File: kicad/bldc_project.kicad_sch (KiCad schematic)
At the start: 33 parts, among them Q1 IRFZ44N, Q2 IRFZ44N, Q3 IRFZ44N, Q4 IRFZ44N, Q5 IRFZ44N, Q6 IRFZ44N, U1 IR2104, U2 IR2104, U3 IR2104

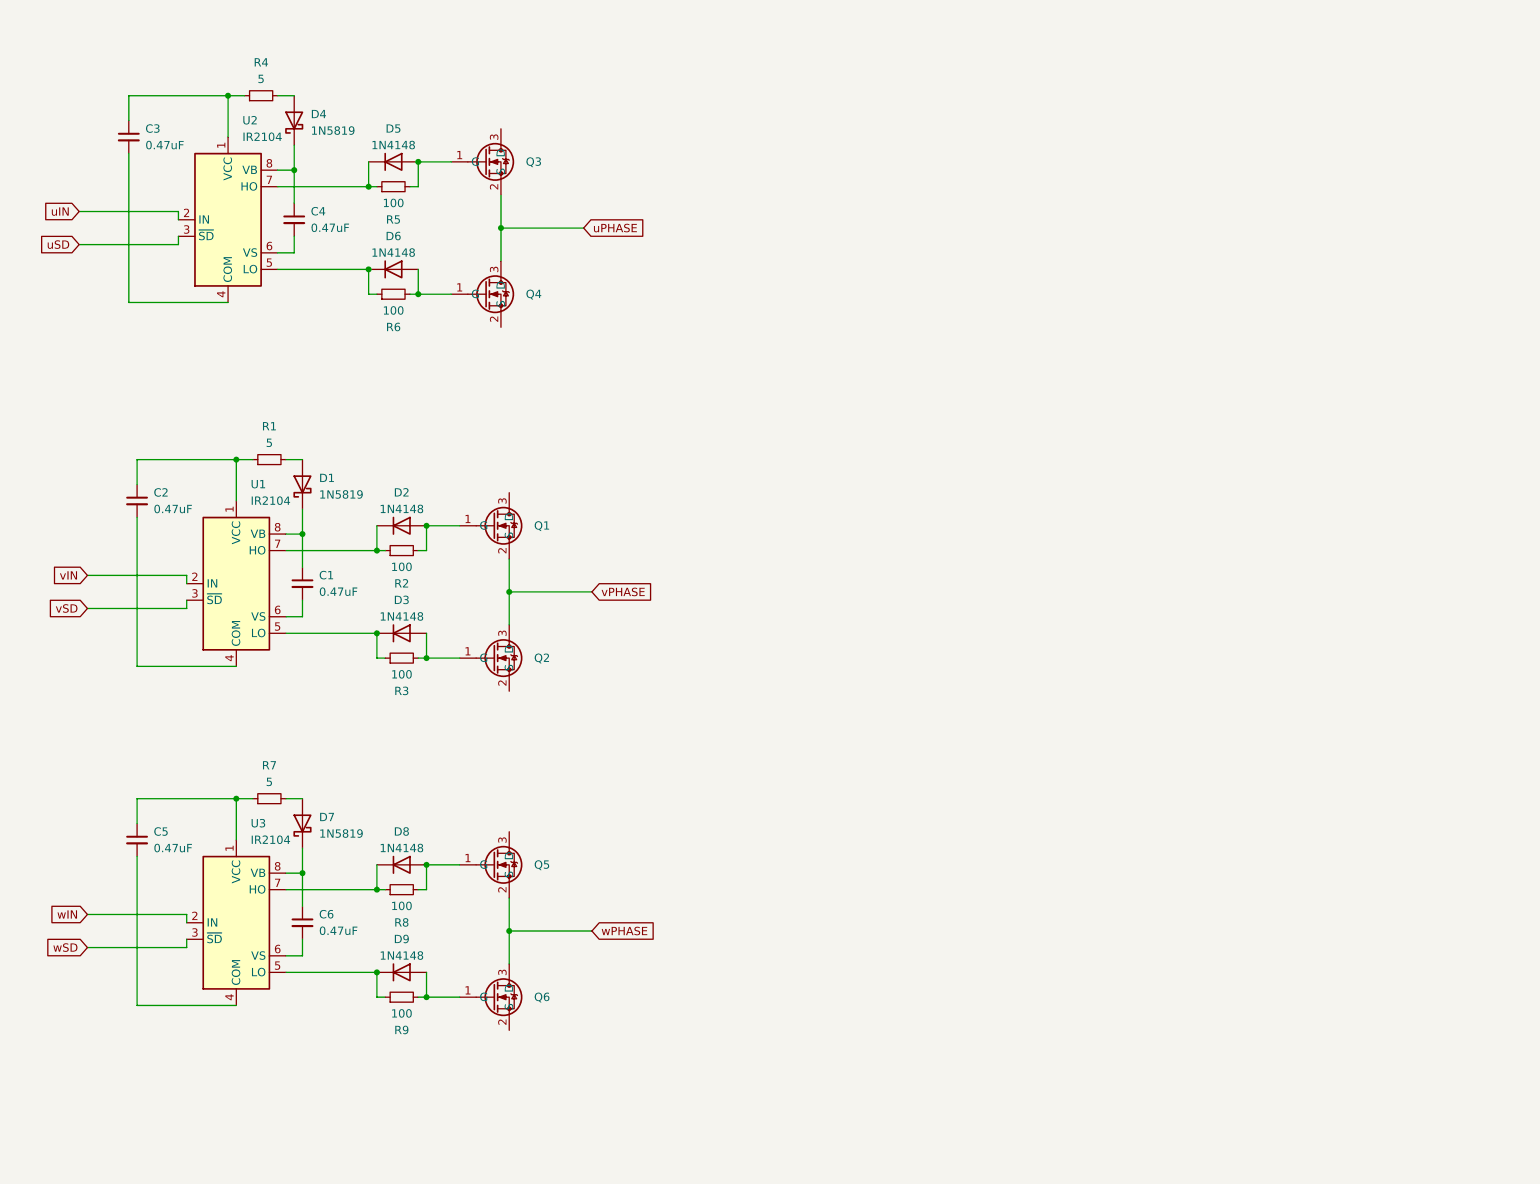
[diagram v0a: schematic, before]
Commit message: [simulations] Simulated 3 OPAMP-circuits + RC filter, chose INA1803A, [kicad] Added current measuring circuit + future todo checks
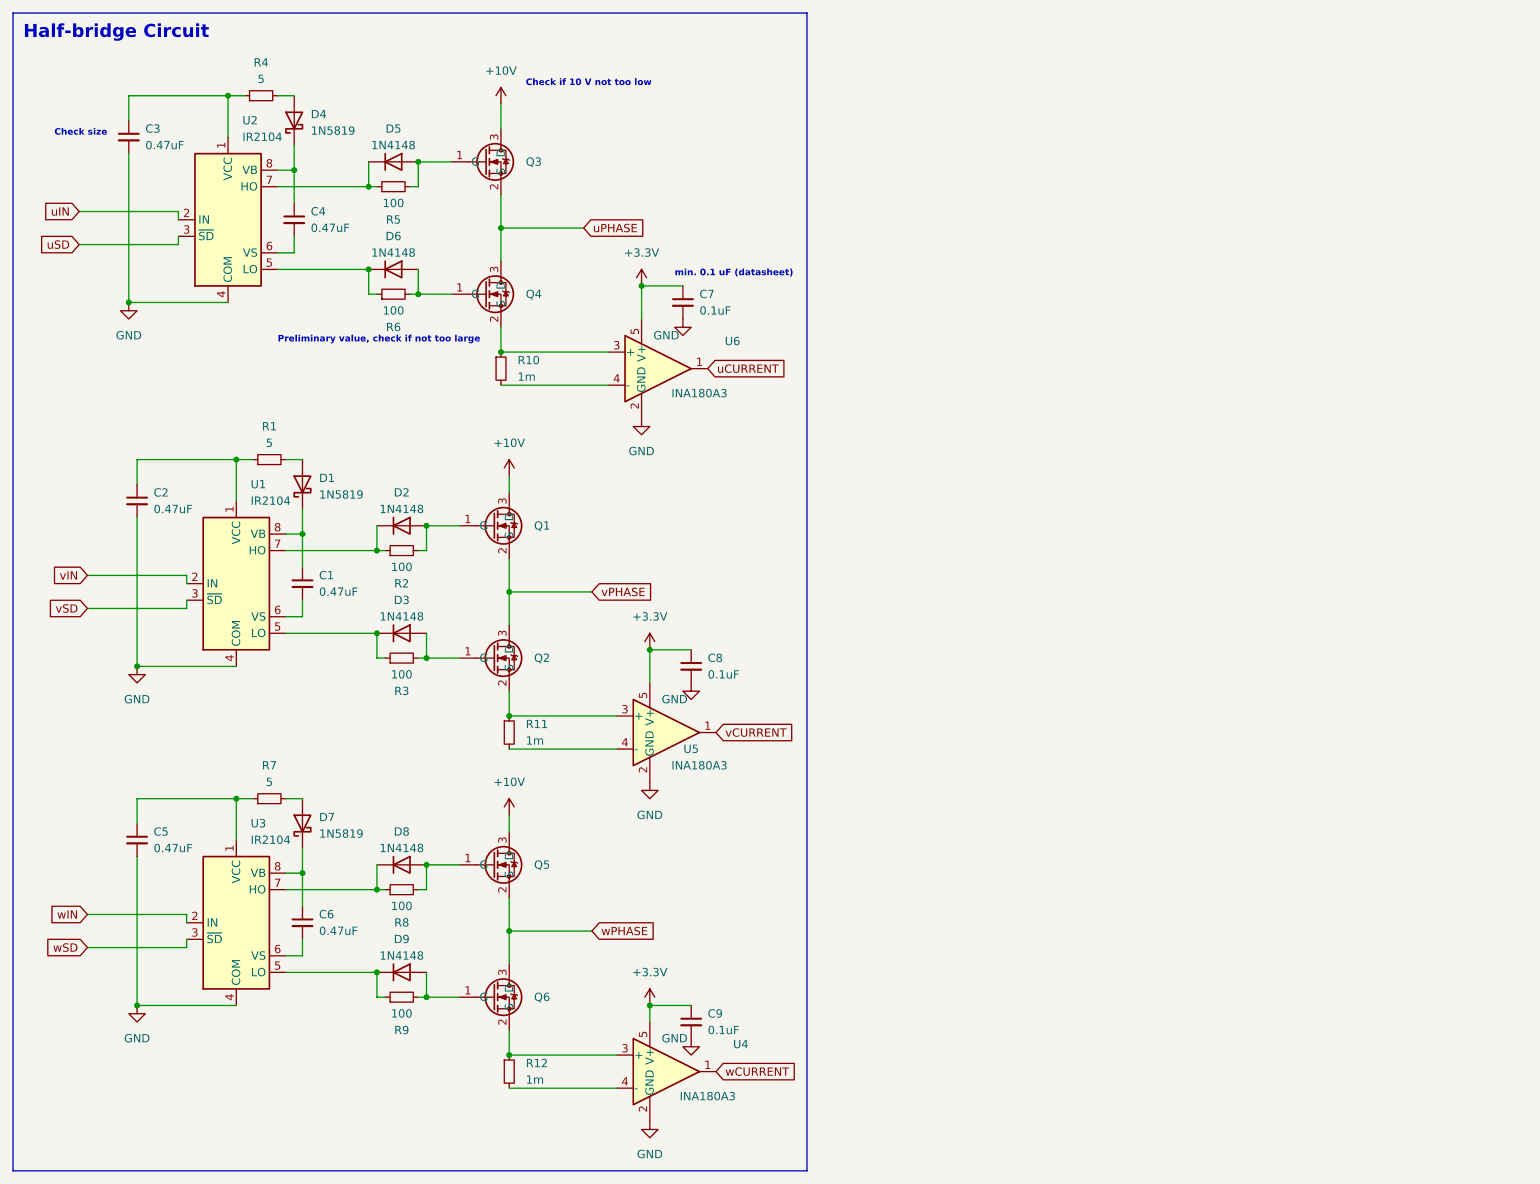
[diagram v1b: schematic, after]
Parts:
- added C7, C8, C9: 0.1uF, symbol Device:C_Small
- added R10, R11, R12: 1m, symbol Device:R_Small
- added U4, U5, U6: INA180A3, Package_TO_SOT_SMD:SOT-23-5, symbol Amplifier_Current:INA180A3
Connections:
- net +10V: now reaches Q1.3 (D)
- net +10V: now also Q3.3 (D), Q5.3 (D)
- net GND: now reaches C5.2, U3.4 (COM)
- net GND: now also C2.2, C3.2, U1.4 (COM), U2.4 (COM), C7.2, C8.2, C9.2, U4.2 (GND), U5.2 (GND), U6.2 (GND)
- net at Q2.2 (S): now also R11.1, U5.3 (+)
- net at Q6.2 (S): now also R12.1, U4.3 (+)
- net at Q4.2 (S): now also R10.1, U6.3 (+)
- new net: R11.2, U5.4 (-)
- new net: R12.2, U4.4 (-)
- new net: R10.2, U6.4 (-)
- new net +3.3V: C7.1, C8.1, C9.1, U4.5 (V+), U5.5 (V+), U6.5 (V+)
- new net uCURRENT: U6.1
- new net vCURRENT: U5.1
- new net wCURRENT: U4.1
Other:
- note added: "Check if 10 V not too low"
- note added: "Check size"
- note added: "Preliminary value, check if not too large"
- note added: "min. 0.1 uF (datasheet)"

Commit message: [kicad] Added extra empty schematic for CPU, temp and ocillator, changed shunt resistors + changed opamp to gain 50 [simulation] added simulation for opamp with gain 50
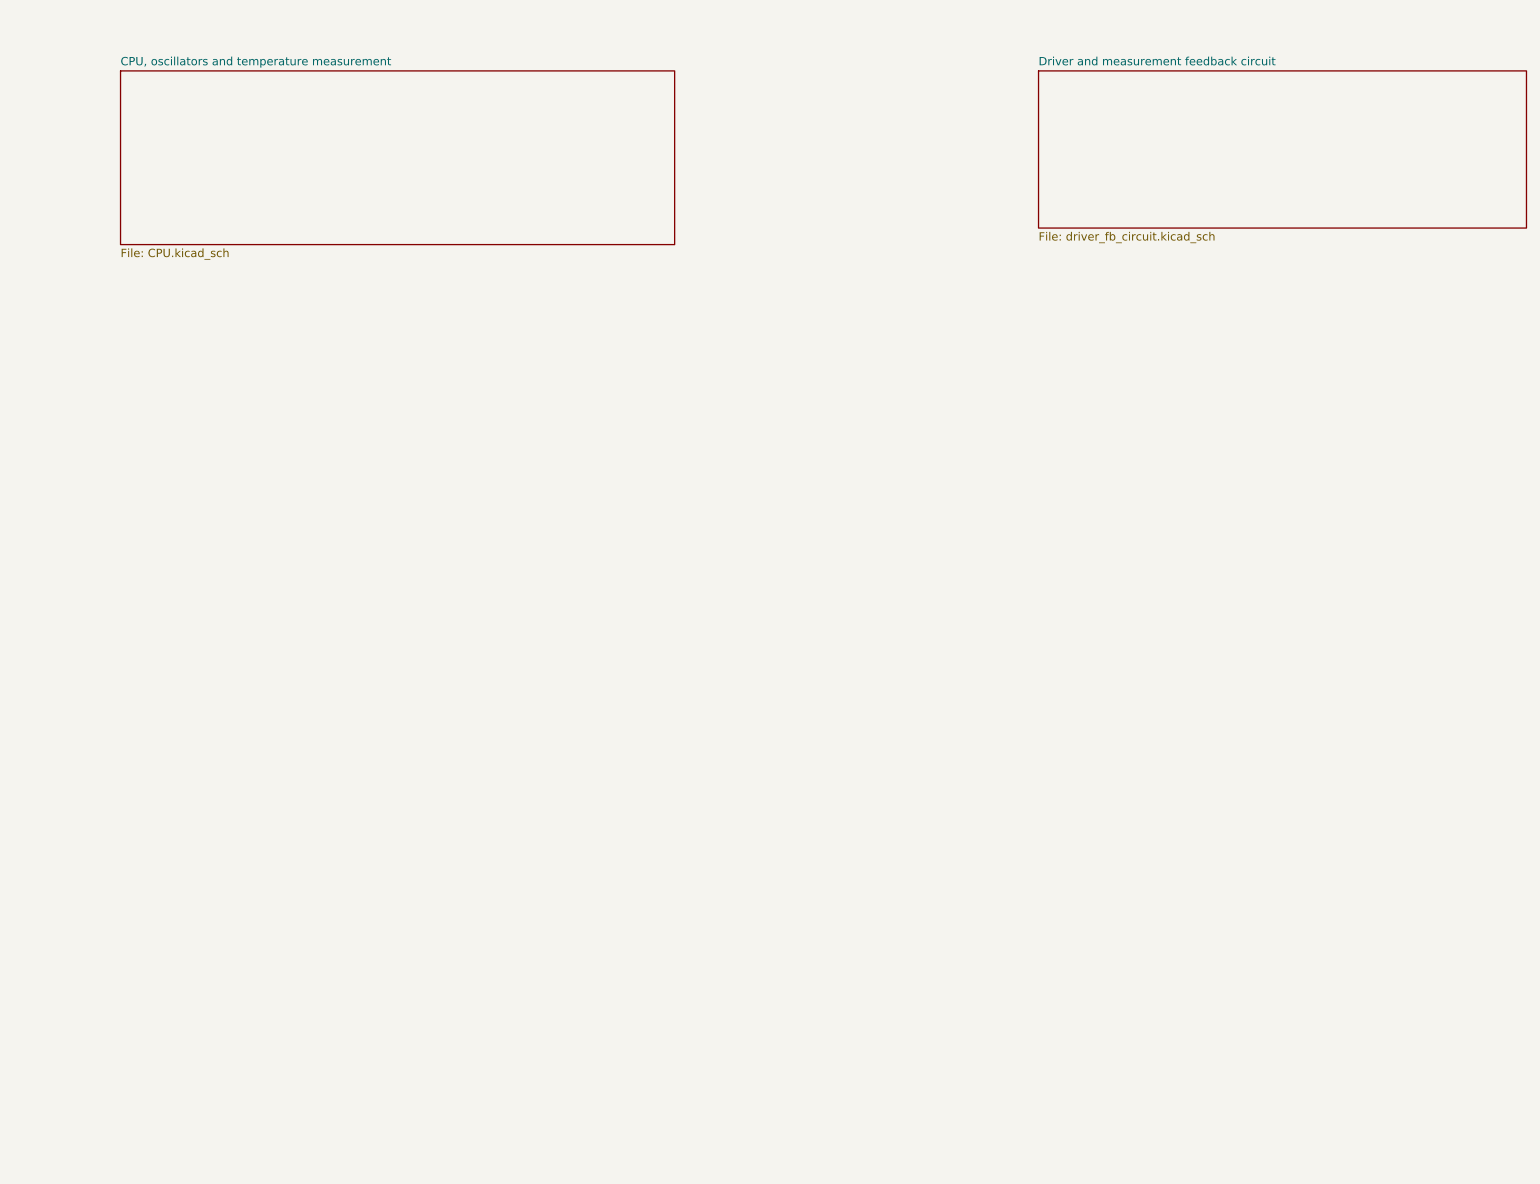
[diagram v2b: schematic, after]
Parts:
- removed C1, C2, C3, C4, C5, C6: 0.47uF, symbol Device:C_Small
- removed C7, C8, C9: 0.1uF, symbol Device:C_Small
- removed D1, D4, D7: 1N5819, Diode_THT:D_DO-41_SOD81_P10.16mm_Horizontal, symbol Diode:1N5819
- removed D2, D3, D5, D6, D8, D9: 1N4148, Diode_THT:D_DO-35_SOD27_P7.62mm_Horizontal, symbol Diode:1N4148
- removed Q1, Q2, Q3, Q4, Q5, Q6: IRFZ44N, Package_TO_SOT_THT:TO-220-3_Vertical, symbol bldc_lib:IRFZ44N
- removed R1, R4, R7: 5, symbol Device:R_Small
- removed R10, R11, R12: 1m, symbol Device:R_Small
- removed R2, R3, R5, R6, R8, R9: 100, symbol Device:R_Small
- removed U1, U2, U3: IR2104, symbol Driver_FET:IR2104
- removed U4, U5, U6: INA180A3, Package_TO_SOT_SMD:SOT-23-5, symbol Amplifier_Current:INA180A3
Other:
- added sheet CPU, oscillators and temperature measurement (CPU.kicad_sch)
- added sheet Driver and measurement feedback circuit (driver_fb_circuit.kicad_sch)
- note removed: "Check if 10 V not too low"
- note removed: "Check size"
- note removed: "Preliminary value, check if not too large"
- note removed: "min. 0.1 uF (datasheet)"
